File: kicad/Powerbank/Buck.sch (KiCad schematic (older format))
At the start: 18 parts, among them SW1 SW_DIP_x01

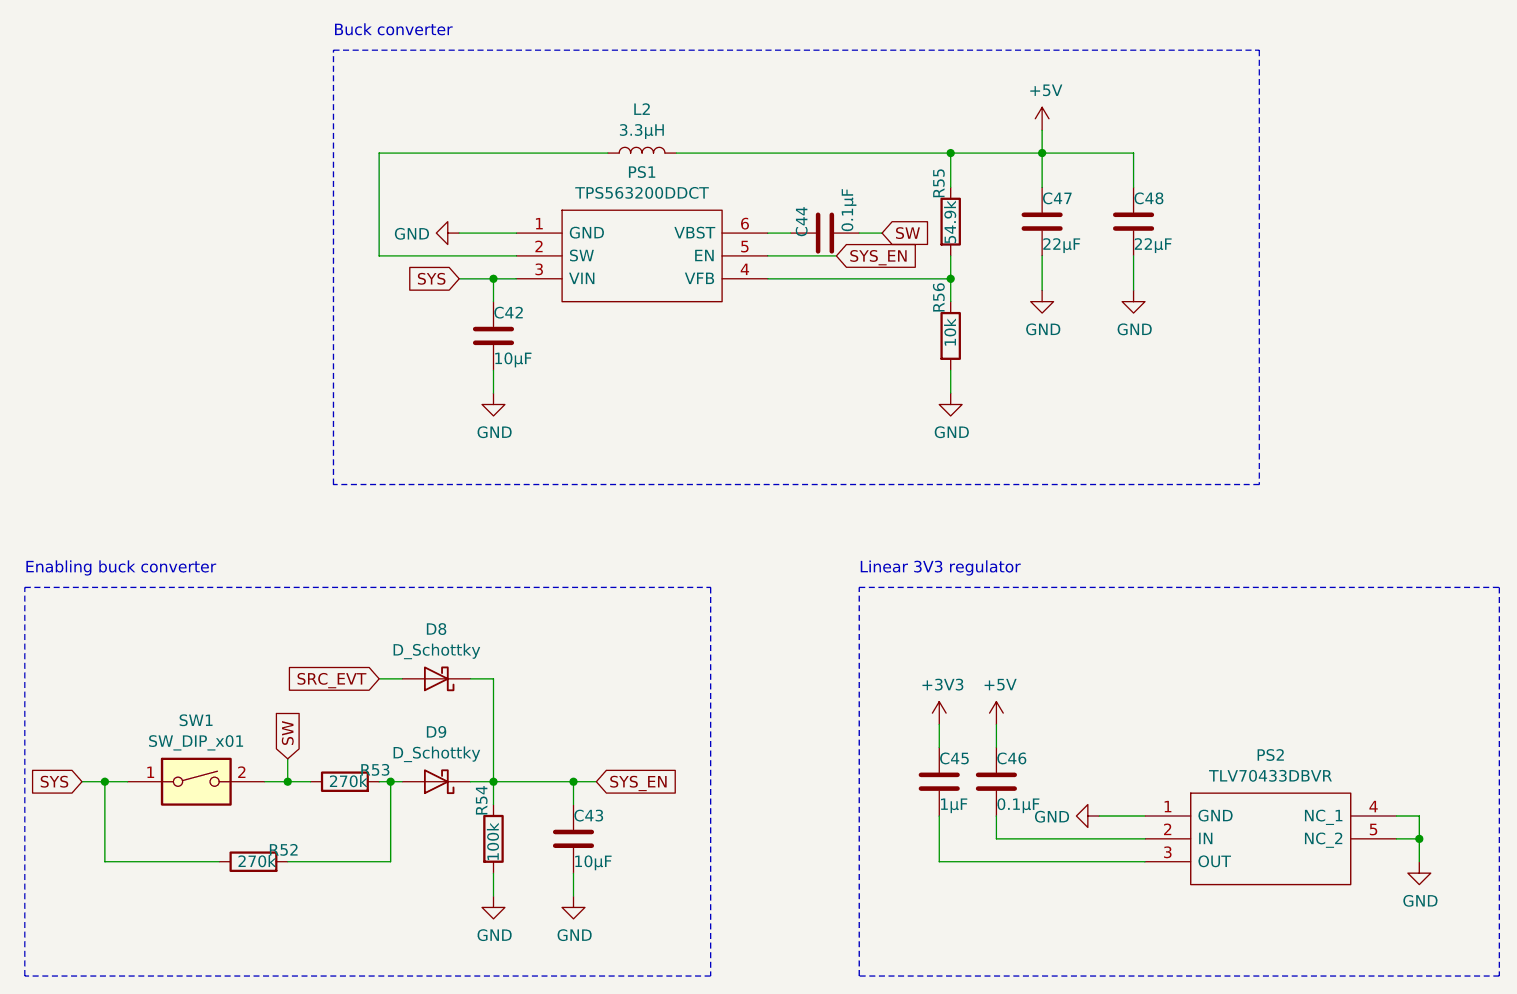
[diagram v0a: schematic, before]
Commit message: Updated layout in schematic for nicer look
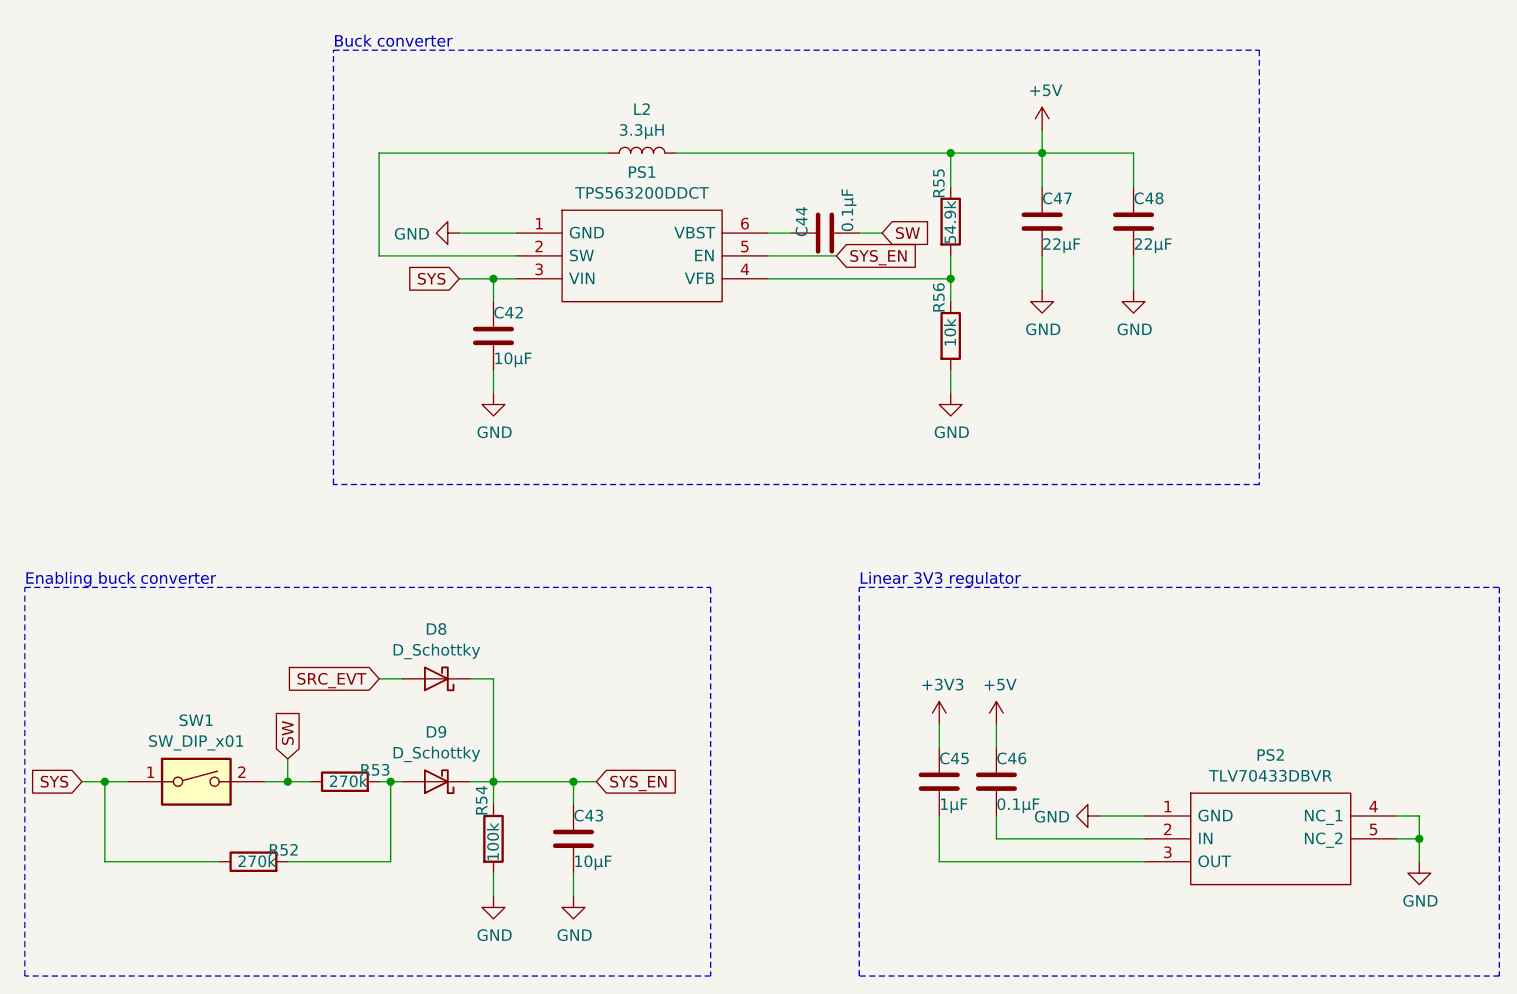
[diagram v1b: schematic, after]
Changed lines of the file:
@@
 $Descr A4 11693 8268
 encoding utf-8
-Sheet 5 7
-Title ""
-Date ""
-Rev ""
+Sheet 4 7
+Title "USB-C PD controller with 4S battery charger"
+Date "2020-01-11"
+Rev "1"
 Comp ""
 Comment1 ""
@@
 Wire Notes Line
 	2600 6200 2600 4500
-Text Notes 2600 4450 0    50   ~ 0
+Text Notes 2600 4500 0    50   ~ 0
 Enabling buck converter
 Wire Notes Line
@@
 Wire Notes Line
 	8000 2150 8000 4050
-Text Notes 3950 2100 0    50   ~ 0
+Text Notes 3950 2150 0    50   ~ 0
 Buck converter
 $Comp
@@
 Wire Notes Line
 	9050 6200 6250 6200
-Text Notes 6250 4450 0    50   ~ 0
+Text Notes 6250 4500 0    50   ~ 0
 Linear 3V3 regulator
 $EndSCHEMATC
